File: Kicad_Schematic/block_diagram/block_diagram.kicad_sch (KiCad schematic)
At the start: 8 parts

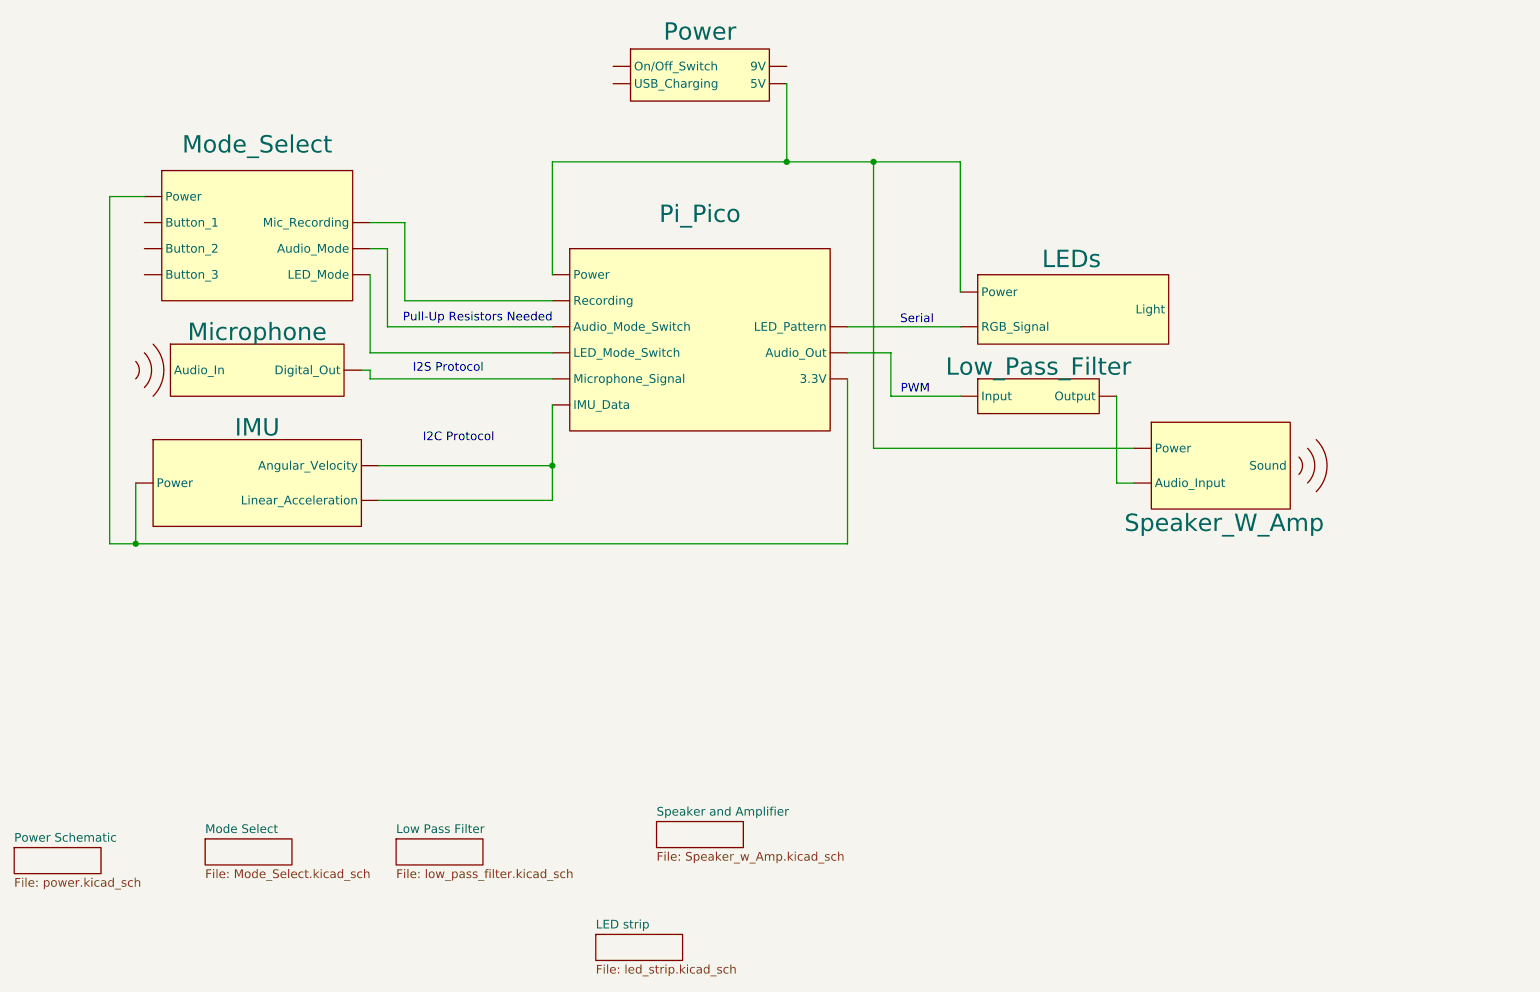
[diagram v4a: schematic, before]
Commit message: edited block diagrams from design rev 2
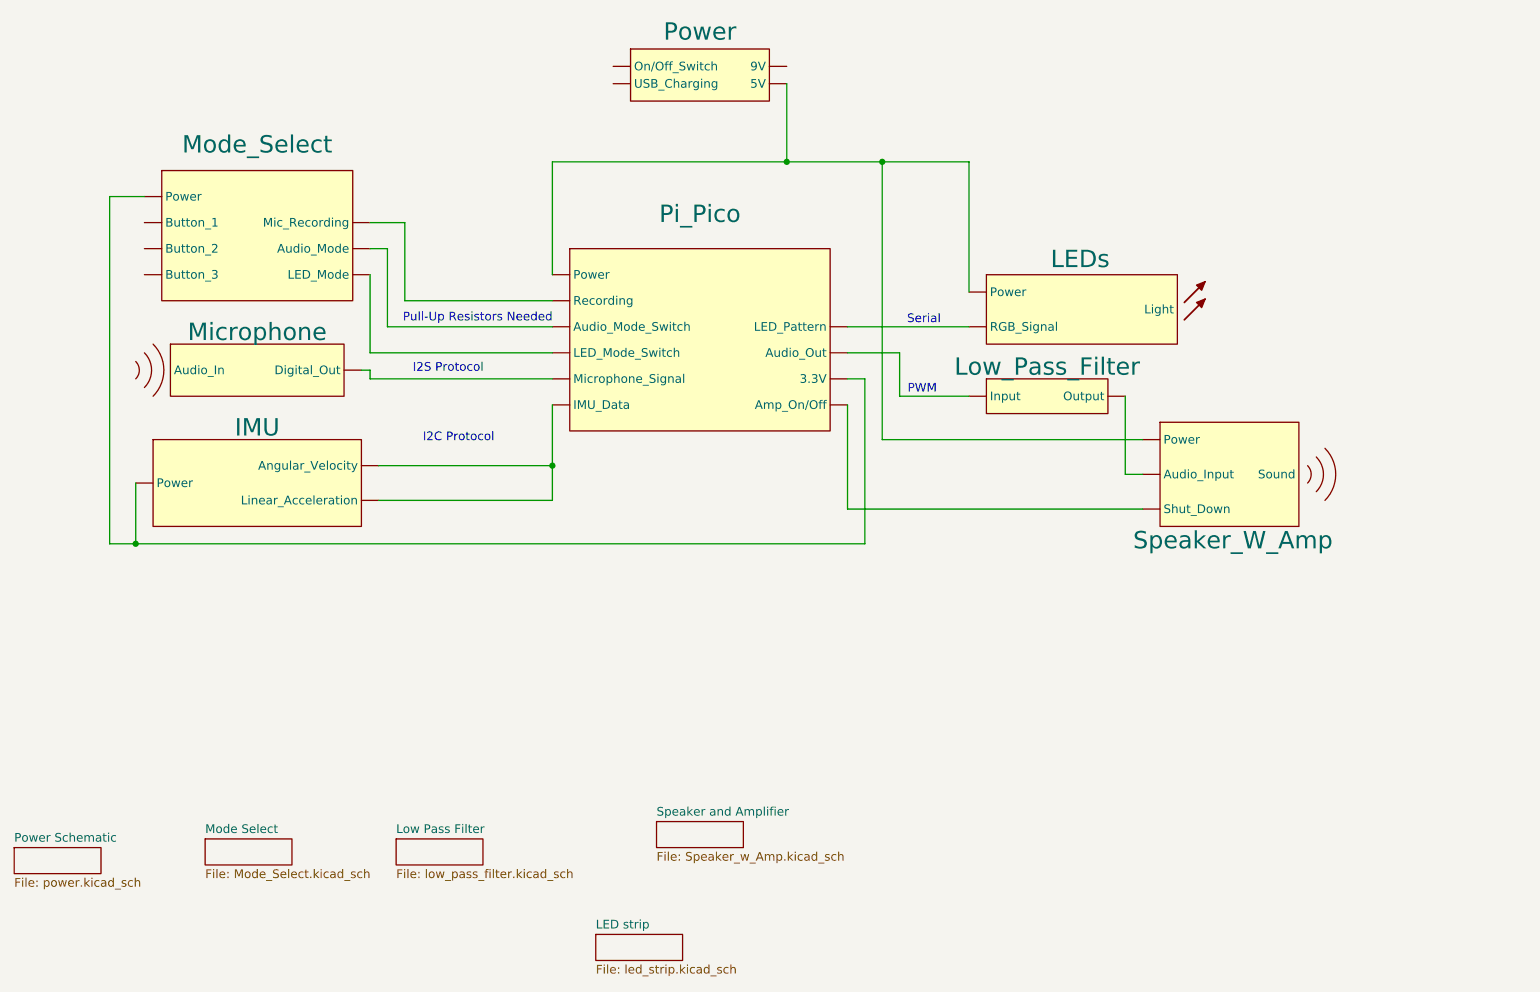
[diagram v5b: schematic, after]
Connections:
- net at Low_Pass_Filter. (Output): now also Speaker_W_Amp. (Sound); no longer Pi_Pico. (3.3V)
- net at Speaker_W_Amp. (Sound): no longer Low_Pass_Filter. (Output)
- net at LEDs. (Light): now also Pi_Pico. (Amp_On/Off), Power. (5V), Speaker_W_Amp. (Sound)
- net at Pi_Pico. (Amp_On/Off): now also Speaker_W_Amp. (Sound); no longer LEDs. (Light)
- net at Mode_Select. (LED_Mode): no longer Pi_Pico. (3.3V)
- net at Microphone. (Digital_Out): no longer Pi_Pico. (3.3V)
- new net: Low_Pass_Filter. (Output), Pi_Pico. (Amp_On/Off)
- new net: LEDs. (Light), Pi_Pico. (Amp_On/Off)
- new net: Mode_Select. (LED_Mode), Pi_Pico. (Amp_On/Off) (x3)
- new net: IMU. (Linear_Acceleration), Mode_Select. (LED_Mode), Pi_Pico. (Amp_On/Off)
- new net: Microphone. (Digital_Out), Pi_Pico. (Amp_On/Off)
- now unconnected: Mode_Select. (LED_Mode), Mode_Select. (LED_Mode), Mode_Select. (LED_Mode), Power. (5V), Speaker_W_Amp. (Sound)
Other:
- moved on the sheet: LEDs, Low_Pass_Filter

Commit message: updated to hw5 block diagram; no more mic, +SD, +LED level shift
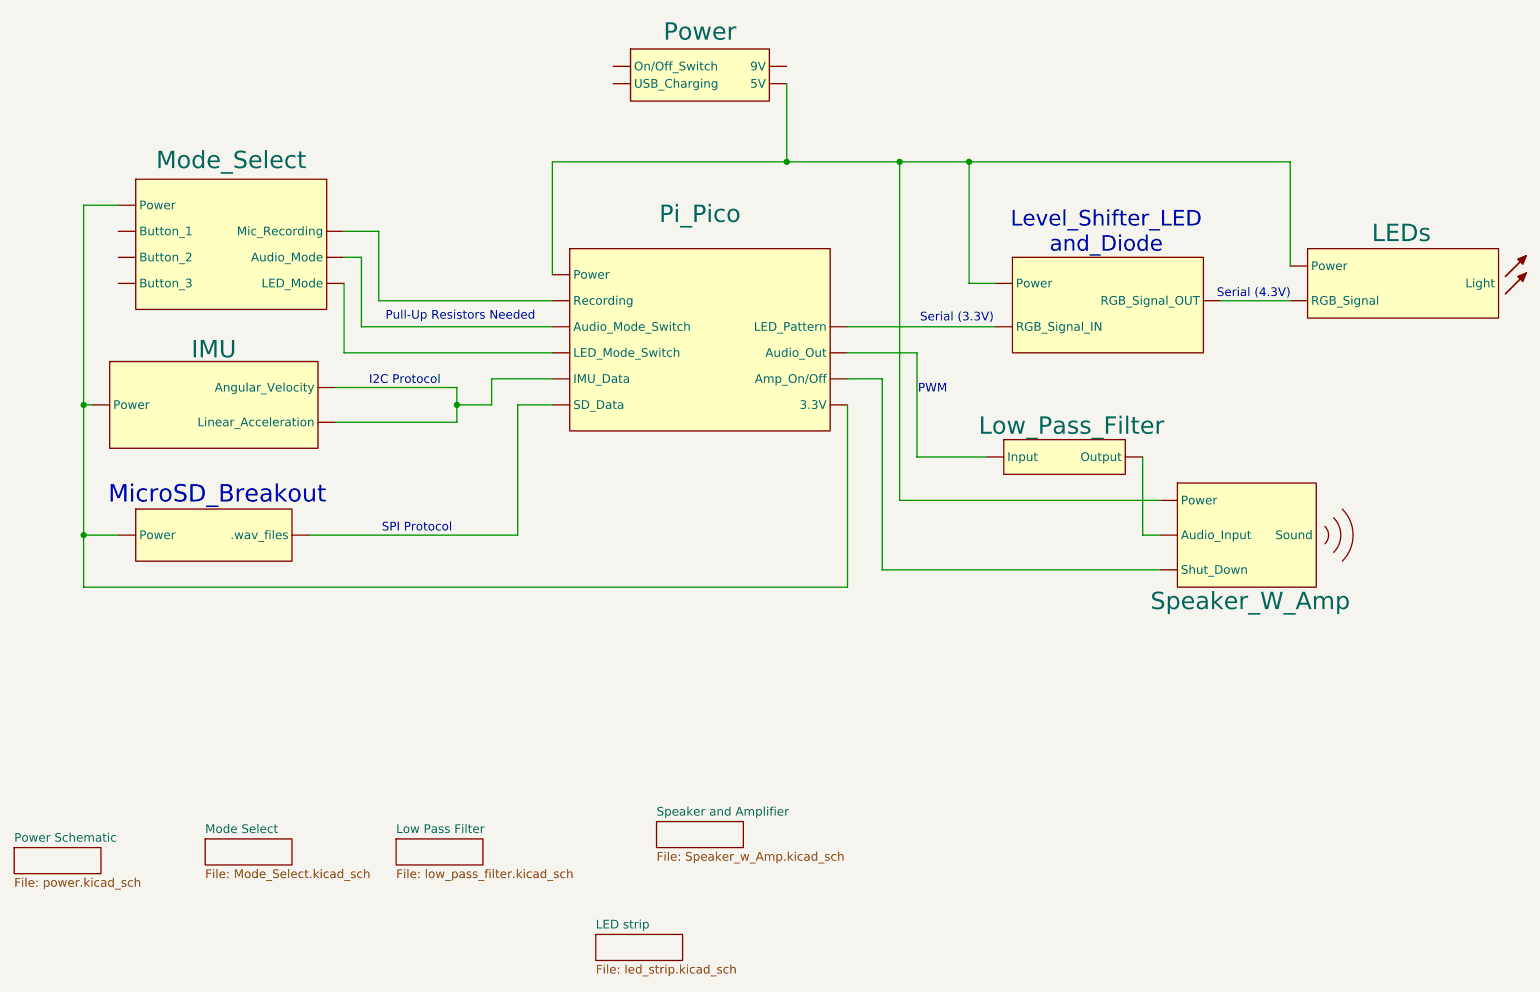
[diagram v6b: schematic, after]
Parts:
- removed Microphone: ~, symbol Block_Diagram_Blocks:Microphone
- added U1: ~, symbol Block_Diagram_Blocks:Level_Shifting_LED
- added U2: ~, symbol Block_Diagram_Blocks:MicroSD_Breakout
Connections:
- net at Low_Pass_Filter. (Output): now also Speaker_W_Amp. (Sound); no longer Pi_Pico. (Amp_On/Off)
- net at Speaker_W_Amp. (Sound): no longer Low_Pass_Filter. (Output)
- net at Pi_Pico. (3.3V): now also Speaker_W_Amp. (Sound); no longer LEDs. (Light)
- net at Mode_Select. (LED_Mode): no longer Pi_Pico. (Amp_On/Off)
- new net: Low_Pass_Filter. (Output), Pi_Pico. (3.3V)
- new net: LEDs. (Light), U1. (RGB_Signal_OUT)
- new net: LEDs. (Light), Pi_Pico. (3.3V), Power. (5V), Speaker_W_Amp. (Sound), U1. (RGB_Signal_OUT)
- new net: Pi_Pico. (3.3V), U1. (RGB_Signal_OUT)
- new net: Mode_Select. (LED_Mode), Pi_Pico. (3.3V) (x3)
- new net: IMU. (Linear_Acceleration), Mode_Select. (LED_Mode), Pi_Pico. (3.3V), U2. (.wav_files)
- new net: Pi_Pico. (3.3V), U2. (.wav_files)
- now unconnected: LEDs. (Light), Mode_Select. (LED_Mode), Mode_Select. (LED_Mode), Mode_Select. (LED_Mode), Power. (5V), Speaker_W_Amp. (Sound), Speaker_W_Amp. (Sound)
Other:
- note added: "Level_Shifter_LED and_Diode"
- note added: "MicroSD_Breakout"
- note added: "SPI Protocol"
- note added: "Serial (3.3V)"
- note added: "Serial (4.3V)"
- note removed: "I2S Protocol"
- note removed: "Serial"
- moved on the sheet: IMU, LEDs, Low_Pass_Filter, Mode_Select, Speaker_W_Amp
